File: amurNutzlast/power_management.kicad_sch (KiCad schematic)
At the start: 14 parts

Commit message: finisched design schematics + pdf
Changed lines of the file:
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@@
   (junction (at 157.48 96.52) (diameter 0) (color 0 0 0 0)
   )
+  (junction (at 177.8 63.5) (diameter 0) (color 0 0 0 0)
+  )
   (junction (at 147.32 96.52) (diameter 0) (color 0 0 0 0)
   )
@@
   (junction (at 45.72 73.66) (diameter 0) (color 0 0 0 0)
   )
+  (junction (at 177.8 96.52) (diameter 0) (color 0 0 0 0)
+  )
   (junction (at 132.08 78.74) (diameter 0) (color 0 0 0 0)
   )
@@
     (stroke (width 0) (type default))
   )
+  (wire (pts (xy 55.88 63.5) (xy 55.88 73.66))
+    (stroke (width 0) (type default))
+  )
   (wire (pts (xy 71.12 73.66) (xy 76.2 73.66))
     (stroke (width 0) (type default))
@@
     (stroke (width 0) (type default))
   )
+  (wire (pts (xy 177.8 96.52) (xy 187.96 96.52))
+    (stroke (width 0) (type default))
+  )
   (wire (pts (xy 71.12 81.28) (xy 71.12 78.74))
     (stroke (width 0) (type default))
@@
     (stroke (width 0) (type default))
   )
+  (wire (pts (xy 187.96 58.42) (xy 187.96 63.5))
+    (stroke (width 0) (type default))
+  )
   (wire (pts (xy 157.48 96.52) (xy 165.1 96.52))
     (stroke (width 0) (type default))
@@
     (stroke (width 0) (type default))
   )
+  (wire (pts (xy 177.8 63.5) (xy 187.96 63.5))
+    (stroke (width 0) (type default))
+  )
   (wire (pts (xy 63.5 73.66) (xy 63.5 86.36))
     (stroke (width 0) (type default))
@@
   )
   (wire (pts (xy 71.12 76.2) (xy 71.12 73.66))
+    (stroke (width 0) (type default))
+  )
+  (wire (pts (xy 187.96 91.44) (xy 187.96 96.52))
     (stroke (width 0) (type default))
   )
@@
     )
   )
+  (symbol (lib_id "power:PWR_FLAG") (at 187.96 91.44 0) (unit 1)
+    (in_bom yes) (on_board yes) (dnp no) (fields_autoplaced)
+    (property "Reference" "#FLG02" (at 187.96 89.535 0)
+      (effects (font (size 1.27 1.27)) hide)
+    )
+    (property "Value" "PWR_FLAG" (at 187.96 86.36 0)
+      (effects (font (size 1.27 1.27)))
+    )
+    (property "Footprint" "" (at 187.96 91.44 0)
+      (effects (font (size 1.27 1.27)) hide)
+    )
+    (property "Datasheet" "~" (at 187.96 91.44 0)
+      (effects (font (size 1.27 1.27)) hide)
+    )
+    (pin "1")
+    (instances
+      (project "amurNutzlast"
+        (path "/81bb76b1-eb1b-4eda-9d04-3f9c2ab6907c/c3ff46ef-9658-4832-9a1d-c566885b7e4f"
+          (reference "#FLG02") (unit 1)
+        )
+      )
+    )
+  )
+  (symbol (lib_id "power:PWR_FLAG") (at 187.96 58.42 0) (unit 1)
+    (in_bom yes) (on_board yes) (dnp no) (fields_autoplaced)
+    (property "Reference" "#FLG01" (at 187.96 56.515 0)
+      (effects (font (size 1.27 1.27)) hide)
+    )
+    (property "Value" "PWR_FLAG" (at 187.96 53.34 0)
+      (effects (font (size 1.27 1.27)))
+    )
+    (property "Footprint" "" (at 187.96 58.42 0)
+      (effects (font (size 1.27 1.27)) hide)
+    )
+    (property "Datasheet" "~" (at 187.96 58.42 0)
+      (effects (font (size 1.27 1.27)) hide)
+    )
+    (pin "1")
+    (instances
+      (project "amurNutzlast"
+        (path "/81bb76b1-eb1b-4eda-9d04-3f9c2ab6907c/c3ff46ef-9658-4832-9a1d-c566885b7e4f"
+          (reference "#FLG01") (unit 1)
+        )
+      )
+    )
+  )
   (symbol (lib_id "Device:R_Small") (at 132.08 68.58 0) (unit 1)
     (in_bom yes) (on_board yes) (dnp no) (fields_autoplaced)
@@
         )
       )
+    )
+  )
+  (symbol (lib_id "power:PWR_FLAG") (at 55.88 63.5 0) (unit 1)
+    (in_bom yes) (on_board yes) (dnp no) (fields_autoplaced)
+    (property "Reference" "#FLG010" (at 55.88 61.595 0)
+      (effects (font (size 1.27 1.27)) hide)
+    )
+    (property "Value" "PWR_FLAG" (at 55.88 58.42 0)
+      (effects (font (size 1.27 1.27)))
+    )
+    (property "Footprint" "" (at 55.88 63.5 0)
+      (effects (font (size 1.27 1.27)) hide)
+    )
+    (property "Datasheet" "~" (at 55.88 63.5 0)
+      (effects (font (size 1.27 1.27)) hide)
+    )
+    (pin "1")
+    (instances
+      (project "amurNutzlast"
+        (path "/81bb76b1-eb1b-4eda-9d04-3f9c2ab6907c/c3ff46ef-9658-4832-9a1d-c566885b7e4f"
+          (reference "#FLG010") (unit 1)
+        )
+      )

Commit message: layout start
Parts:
- C19, C20, C21, C22, C23: footprint (none) -> Capacitor_SMD:C_0603_1608Metric
- R10, R11, R12, R13, R14, R7, R8, R9: footprint (none) -> Resistor_SMD:R_0603_1608Metric
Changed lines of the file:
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@@
       (effects (font (size 1.27 1.27)) (justify left))
     )
-    (property "Footprint" "" (at 119.38 99.06 0)
+    (property "Footprint" "Capacitor_SMD:C_0603_1608Metric" (at 119.38 99.06 0)
       (effects (font (size 1.27 1.27)) hide)
     )
@@
       (effects (font (size 1.27 1.27)) (justify left))
     )
-    (property "Footprint" "" (at 63.5 88.9 0)
+    (property "Footprint" "Resistor_SMD:R_0603_1608Metric" (at 63.5 88.9 0)
       (effects (font (size 1.27 1.27)) hide)
     )
@@
       (effects (font (size 1.27 1.27)) (justify left))
     )
-    (property "Footprint" "" (at 45.72 81.28 0)
+    (property "Footprint" "Capacitor_SMD:C_0603_1608Metric" (at 45.72 81.28 0)
       (effects (font (size 1.27 1.27)) hide)
     )
@@
       (effects (font (size 1.27 1.27)))
     )
-    (property "Footprint" "" (at 167.64 96.52 0)
+    (property "Footprint" "Resistor_SMD:R_0603_1608Metric" (at 167.64 96.52 0)
       (effects (font (size 1.27 1.27)) hide)
     )
@@
       (effects (font (size 1.27 1.27)) (justify right))
     )
-    (property "Footprint" "" (at 160.02 71.12 0)
+    (property "Footprint" "Resistor_SMD:R_0603_1608Metric" (at 160.02 71.12 0)
       (effects (font (size 1.27 1.27)) hide)
     )
@@
       (effects (font (size 1.27 1.27)) (justify left))
     )
-    (property "Footprint" "" (at 55.88 88.9 0)
+    (property "Footprint" "Resistor_SMD:R_0603_1608Metric" (at 55.88 88.9 0)
       (effects (font (size 1.27 1.27)) hide)
     )
@@
       (effects (font (size 1.27 1.27)) (justify left))
     )
-    (property "Footprint" "" (at 119.38 66.04 0)
+    (property "Footprint" "Capacitor_SMD:C_0603_1608Metric" (at 119.38 66.04 0)
       (effects (font (size 1.27 1.27)) hide)
     )
@@
       (effects (font (size 1.27 1.27)) (justify left))
     )
-    (property "Footprint" "" (at 132.08 68.58 0)
+    (property "Footprint" "Resistor_SMD:R_0603_1608Metric" (at 132.08 68.58 0)
       (effects (font (size 1.27 1.27)) hide)
     )
@@
       (effects (font (size 1.27 1.27)))
     )
-    (property "Footprint" "" (at 170.18 63.5 0)
+    (property "Footprint" "Resistor_SMD:R_0603_1608Metric" (at 170.18 63.5 0)
       (effects (font (size 1.27 1.27)) hide)
     )
@@
       (effects (font (size 1.27 1.27)) (justify left))
     )
-    (property "Footprint" "" (at 157.48 104.14 0)
+    (property "Footprint" "Resistor_SMD:R_0603_1608Metric" (at 157.48 104.14 0)
       (effects (font (size 1.27 1.27)) hide)
     )
@@
       (effects (font (size 1.27 1.27)))
     )
-    (property "Footprint" "" (at 142.24 78.74 0)
+    (property "Footprint" "Resistor_SMD:R_0603_1608Metric" (at 142.24 78.74 0)
       (effects (font (size 1.27 1.27)) hide)
     )
@@
       (effects (font (size 1.27 1.27)) (justify left))
     )
-    (property "Footprint" "" (at 149.86 68.58 0)
+    (property "Footprint" "Capacitor_SMD:C_0603_1608Metric" (at 149.86 68.58 0)
       (effects (font (size 1.27 1.27)) hide)
     )
@@
       (effects (font (size 1.27 1.27)) (justify left))
     )
-    (property "Footprint" "" (at 147.32 104.14 0)
-      (effects (font (size 1.27 1.27)) hide)
-    )
+    (property "Footprint" "Capacitor_SMD:C_0603_1608Metric" (at 147.32 104.14 0)
+      (effects (font (size 1.27 1.27)) hide)
+    )

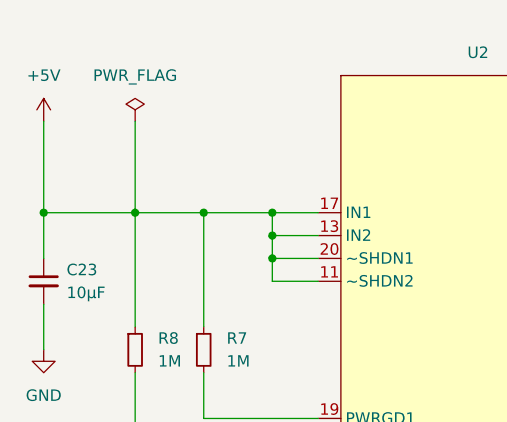
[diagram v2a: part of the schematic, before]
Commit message: deleted 3.3 converter for ftdi and moved USB to a hierarhical sheet
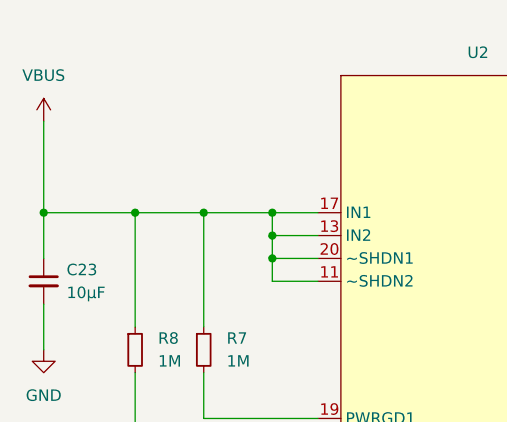
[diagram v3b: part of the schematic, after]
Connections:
- net +5V renamed VBUS
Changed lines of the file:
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@@
-    (stroke (width 0) (type default))
-  )
-  (wire (pts (xy 55.88 63.5) (xy 55.88 73.66))
     (stroke (width 0) (type default))
   )
@@
         (path "/81bb76b1-eb1b-4eda-9d04-3f9c2ab6907c/c3ff46ef-9658-4832-9a1d-c566885b7e4f"
           (reference "#PWR044") (unit 1)
-        )
-      )
-    )
-  )
-  (symbol (lib_id "power:+5V") (at 45.72 63.5 0) (unit 1)
-    (in_bom yes) (on_board yes) (dnp no) (fields_autoplaced)
-    (property "Reference" "#PWR043" (at 45.72 67.31 0)
-      (effects (font (size 1.27 1.27)) hide)
-    )
-    (property "Value" "+5V" (at 45.72 58.42 0)
-      (effects (font (size 1.27 1.27)))
-    )
-    (property "Footprint" "" (at 45.72 63.5 0)
-      (effects (font (size 1.27 1.27)) hide)
-    )
-    (property "Datasheet" "" (at 45.72 63.5 0)
-      (effects (font (size 1.27 1.27)) hide)
-    )
-    (pin "1")
-    (instances
-      (project "amurNutzlast"
-        (path "/81bb76b1-eb1b-4eda-9d04-3f9c2ab6907c/c3ff46ef-9658-4832-9a1d-c566885b7e4f"
-          (reference "#PWR043") (unit 1)
         )
       )
@@
     )
   )
-  (symbol (lib_id "power:PWR_FLAG") (at 55.88 63.5 0) (unit 1)
-    (in_bom yes) (on_board yes) (dnp no) (fields_autoplaced)
-    (property "Reference" "#FLG010" (at 55.88 61.595 0)
-      (effects (font (size 1.27 1.27)) hide)
-    )
-    (property "Value" "PWR_FLAG" (at 55.88 58.42 0)
-      (effects (font (size 1.27 1.27)))
-    )
-    (property "Footprint" "" (at 55.88 63.5 0)
-      (effects (font (size 1.27 1.27)) hide)
-    )
-    (property "Datasheet" "~" (at 55.88 63.5 0)
-      (effects (font (size 1.27 1.27)) hide)
-    )
-    (pin "1")
-    (instances
-      (project "amurNutzlast"
-        (path "/81bb76b1-eb1b-4eda-9d04-3f9c2ab6907c/c3ff46ef-9658-4832-9a1d-c566885b7e4f"
-          (reference "#FLG010") (unit 1)
-        )
-      )
+  (symbol (lib_id "power:VBUS") (at 45.72 63.5 0) (unit 1)
+    (in_bom yes) (on_board yes) (dnp no) (fields_autoplaced)
+    (property "Reference" "#PWR043" (at 45.72 67.31 0)
+      (effects (font (size 1.27 1.27)) hide)
+    )
+    (property "Value" "VBUS" (at 45.72 58.42 0)
+      (effects (font (size 1.27 1.27)))
+    )
+    (property "Footprint" "" (at 45.72 63.5 0)
+      (effects (font (size 1.27 1.27)) hide)
+    )
+    (property "Datasheet" "" (at 45.72 63.5 0)
+      (effects (font (size 1.27 1.27)) hide)
+    )
+    (pin "1")
+    (instances
+      (project "amurNutzlast"
+        (path "/81bb76b1-eb1b-4eda-9d04-3f9c2ab6907c/c3ff46ef-9658-4832-9a1d-c566885b7e4f"
+          (reference "#PWR043") (unit 1)
+        )
+      )

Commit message: layout ftdi placement
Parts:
- added C40: 0.1µF, Capacitor_SMD:C_0603_1608Metric, symbol Device:C_Small
- added C41: 10µF, Capacitor_SMD:C_0603_1608Metric, symbol Device:C_Small
- added U3: LD1117S33TR_SOT223, Package_TO_SOT_SMD:SOT-223-3_TabPin2, symbol Regulator_Linear:LD1117S33TR_SOT223
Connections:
- net VBUS: now also C40.1, U3.3 (VI); no longer C23.1, R7.1, R8.1, U2.11 (~SHDN2), U2.13 (IN2), U2.14 (IN2), U2.17 (IN1), U2.18 (IN1), U2.20 (~SHDN1)
- new net +3.3VP: C41.1, U3.2 (VO)
- new net +5V: C23.1, R7.1, R8.1, U2.11 (~SHDN2), U2.13 (IN2), U2.14 (IN2), U2.17 (IN1), U2.18 (IN1), U2.20 (~SHDN1)
- new net GND1: C40.2, C41.2, U3.1 (GND)

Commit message: placement finished
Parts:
- added J2: Conn_02x02_Counter_Clockwise, Connector_PinHeader_2.54mm:PinHeader_2x02_P2.54mm_Vertical, symbol Connector_Generic:Conn_02x02_Counter_Clockwise
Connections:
- net +5V: now also J2.2 (Pin_2)
- net GND: now also J2.4 (Pin_4)
- net GND1: now also J2.3 (Pin_3)
- net VBUS: now also J2.1 (Pin_1)
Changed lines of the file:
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@@
+    (stroke (width 0) (type default))
+  )
+  (wire (pts (xy 58.42 25.4) (xy 60.96 25.4))
     (stroke (width 0) (type default))
   )
@@
     (stroke (width 0) (type default))
   )
+  (wire (pts (xy 53.34 27.94) (xy 53.34 22.86))
+    (stroke (width 0) (type default))
+  )
   (wire (pts (xy 45.72 50.8) (xy 45.72 73.66))
     (stroke (width 0) (type default))
@@
     (stroke (width 0) (type default))
   )
+  (wire (pts (xy 81.28 30.48) (xy 81.28 25.4))
+    (stroke (width 0) (type default))
+  )
   (wire (pts (xy 73.66 157.48) (xy 81.28 157.48))
     (stroke (width 0) (type default))
@@
     (stroke (width 0) (type default))
   )
+  (wire (pts (xy 76.2 30.48) (xy 76.2 27.94))
+    (stroke (width 0) (type default))
+  )
   (wire (pts (xy 147.32 96.52) (xy 157.48 96.52))
     (stroke (width 0) (type default))
@@
     (stroke (width 0) (type default))
   )
+  (wire (pts (xy 76.2 27.94) (xy 73.66 27.94))
+    (stroke (width 0) (type default))
+  )
   (wire (pts (xy 73.66 165.1) (xy 73.66 167.64))
     (stroke (width 0) (type default))
@@
     (stroke (width 0) (type default))
   )
+  (wire (pts (xy 73.66 25.4) (xy 81.28 25.4))
+    (stroke (width 0) (type default))
+  )
   (wire (pts (xy 111.76 63.5) (xy 119.38 63.5))
     (stroke (width 0) (type default))
@@
     (stroke (width 0) (type default))
   )
+  (wire (pts (xy 53.34 27.94) (xy 60.96 27.94))
+    (stroke (width 0) (type default))
+  )
   (wire (pts (xy 129.54 96.52) (xy 147.32 96.52))
     (stroke (width 0) (type default))
   )
+  (wire (pts (xy 58.42 22.86) (xy 58.42 25.4))
+    (stroke (width 0) (type default))
+  )
   (wire (pts (xy 111.76 96.52) (xy 119.38 96.52))
     (stroke (width 0) (type default))
@@
         (path "/81bb76b1-eb1b-4eda-9d04-3f9c2ab6907c/c3ff46ef-9658-4832-9a1d-c566885b7e4f"
           (reference "C23") (unit 1)
+        )
+      )
+    )
+  )
+  (symbol (lib_id "power:VBUS") (at 58.42 22.86 0) (unit 1)
+    (in_bom yes) (on_board yes) (dnp no) (fields_autoplaced)
+    (property "Reference" "#PWR097" (at 58.42 26.67 0)
+      (effects (font (size 1.27 1.27)) hide)
+    )
+    (property "Value" "VBUS" (at 58.42 17.78 0)
+      (effects (font (size 1.27 1.27)))
+    )
+    (property "Footprint" "" (at 58.42 22.86 0)
+      (effects (font (size 1.27 1.27)) hide)
+    )
+    (property "Datasheet" "" (at 58.42 22.86 0)
+      (effects (font (size 1.27 1.27)) hide)
+    )
+    (pin "1")
+    (instances
+      (project "amurNutzlast"
+        (path "/81bb76b1-eb1b-4eda-9d04-3f9c2ab6907c/c3ff46ef-9658-4832-9a1d-c566885b7e4f"
+          (reference "#PWR097") (unit 1)
         )
       )
@@
     )
   )
+  (symbol (lib_id "Connector_Generic:Conn_02x02_Counter_Clockwise") (at 66.04 25.4 0) (unit 1)
+    (in_bom yes) (on_board yes) (dnp no)
+    (property "Reference" "J2" (at 67.31 19.05 0)
+      (effects (font (size 1.27 1.27)))
+    )
+    (property "Value" "Conn_02x02_Counter_Clockwise" (at 68.58 43.18 0)
+      (effects (font (size 1.27 1.27)))
+    )
+    (property "Footprint" "Connector_PinHeader_2.54mm:PinHeader_2x02_P2.54mm_Vertical" (at 66.04 25.4 0)
+      (effects (font (size 1.27 1.27)) hide)
+    )
+    (property "Datasheet" "~" (at 66.04 25.4 0)
+      (effects (font (size 1.27 1.27)) hide)
+    )
+    (pin "1")
+    (pin "2")
+    (pin "3")
+    (pin "4")
+    (instances
+      (project "amurNutzlast"
+        (path "/81bb76b1-eb1b-4eda-9d04-3f9c2ab6907c/c3ff46ef-9658-4832-9a1d-c566885b7e4f"
+          (reference "J2") (unit 1)
+        )
+      )
+    )
+  )
   (symbol (lib_id "power:GND") (at 157.48 114.3 0) (unit 1)
     (in_bom yes) (on_board yes) (dnp no) (fields_autoplaced)
@@
         (path "/81bb76b1-eb1b-4eda-9d04-3f9c2ab6907c/c3ff46ef-9658-4832-9a1d-c566885b7e4f"
           (reference "C39") (unit 1)
+        )
+      )
+    )
+  )
+  (symbol (lib_id "power:+5V") (at 53.34 22.86 0) (unit 1)
+    (in_bom yes) (on_board yes) (dnp no) (fields_autoplaced)
+    (property "Reference" "#PWR098" (at 53.34 26.67 0)
+      (effects (font (size 1.27 1.27)) hide)
+    )
+    (property "Value" "+5V" (at 53.34 17.78 0)
+      (effects (font (size 1.27 1.27)))
+    )
+    (property "Footprint" "" (at 53.34 22.86 0)
+      (effects (font (size 1.27 1.27)) hide)
+    )
+    (property "Datasheet" "" (at 53.34 22.86 0)
+      (effects (font (size 1.27 1.27)) hide)
+    )
+    (pin "1")
+    (instances
+      (project "amurNutzlast"
+        (path "/81bb76b1-eb1b-4eda-9d04-3f9c2ab6907c/c3ff46ef-9658-4832-9a1d-c566885b7e4f"
+          (reference "#PWR098") (unit 1)
         )
       )
@@
     )
   )
+  (symbol (lib_id "power:GND") (at 81.28 30.48 0) (unit 1)
+    (in_bom yes) (on_board yes) (dnp no) (fields_autoplaced)
+    (property "Reference" "#PWR099" (at 81.28 36.83 0)
+      (effects (font (size 1.27 1.27)) hide)
+    )
+    (property "Value" "GND" (at 81.28 35.56 0)
+      (effects (font (size 1.27 1.27)))
+    )
+    (property "Footprint" "" (at 81.28 30.48 0)
+      (effects (font (size 1.27 1.27)) hide)
+    )
+    (property "Datasheet" "" (at 81.28 30.48 0)
+      (effects (font (size 1.27 1.27)) hide)
+    )
+    (pin "1")
+    (instances
+      (project "amurNutzlast"
+        (path "/81bb76b1-eb1b-4eda-9d04-3f9c2ab6907c/c3ff46ef-9658-4832-9a1d-c566885b7e4f"
+          (reference "#PWR099") (unit 1)
+        )
+      )
+    )
+  )
   (symbol (lib_id "power:+5V") (at 45.72 50.8 0) (unit 1)
     (in_bom yes) (on_board yes) (dnp no) (fields_autoplaced)
@@
         )
       )
+    )
+  )
+  (symbol (lib_id "power:GND1") (at 76.2 30.48 0) (unit 1)
+    (in_bom yes) (on_board yes) (dnp no) (fields_autoplaced)
+    (property "Reference" "#PWR0100" (at 76.2 36.83 0)
+      (effects (font (size 1.27 1.27)) hide)
+    )
+    (property "Value" "GND1" (at 76.2 35.56 0)
+      (effects (font (size 1.27 1.27)))
+    )
+    (property "Footprint" "" (at 76.2 30.48 0)
+      (effects (font (size 1.27 1.27)) hide)
+    )
+    (property "Datasheet" "" (at 76.2 30.48 0)
+      (effects (font (size 1.27 1.27)) hide)
+    )
+    (pin "1")
+    (instances
+      (project "amurNutzlast"
+        (path "/81bb76b1-eb1b-4eda-9d04-3f9c2ab6907c/c3ff46ef-9658-4832-9a1d-c566885b7e4f"
+          (reference "#PWR0100") (unit 1)
+        )
+      )

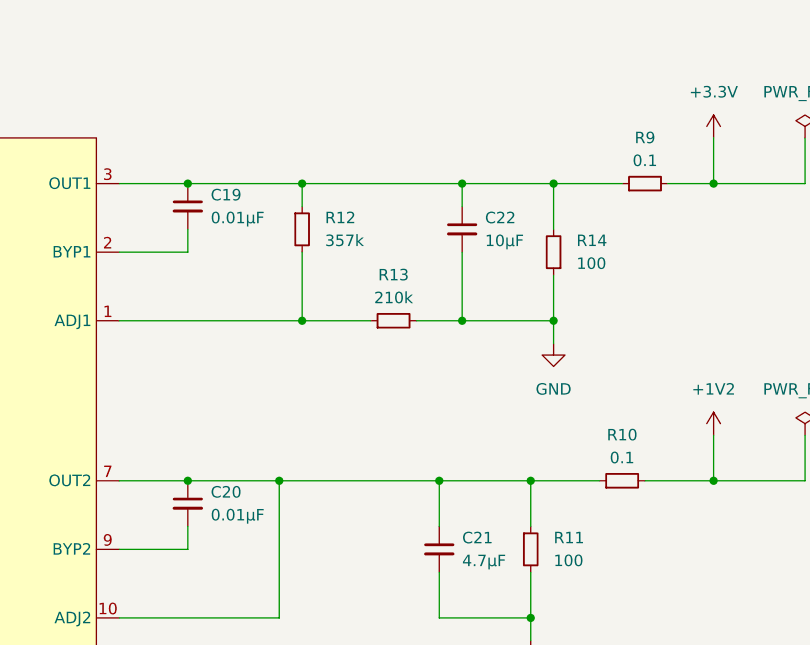
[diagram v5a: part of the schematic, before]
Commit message: gpio connected
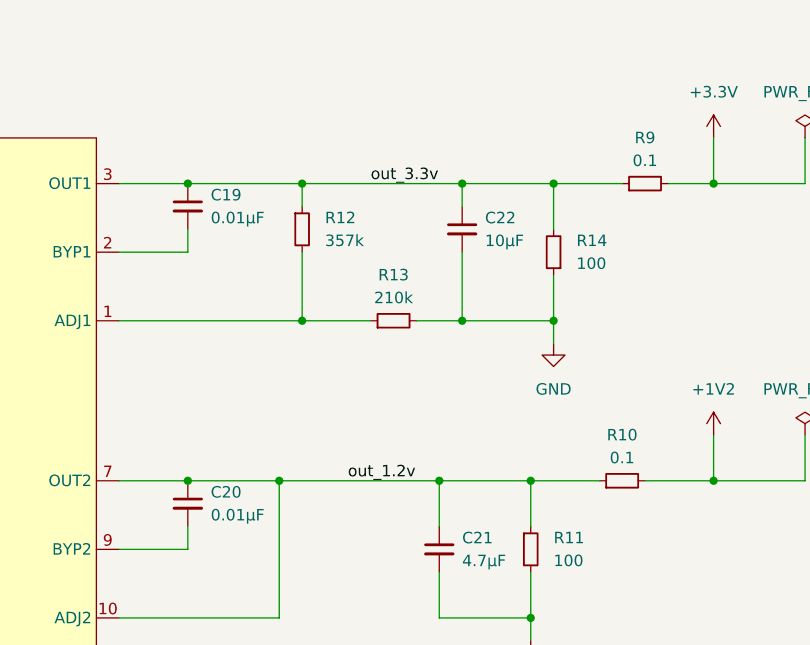
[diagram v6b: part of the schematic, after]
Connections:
- net out_1.2v: now reaches C20.1, C21.1, R10.1, R11.1, U2.10 (ADJ2), U2.7 (OUT2), U2.8 (OUT2)
- net out_3.3v: now reaches C19.1, C22.1, R12.1, R14.2, R9.1, U2.3 (OUT1), U2.4 (OUT1)
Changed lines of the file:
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@@
     (stroke (width 0) (type default))
+  )
+  (label "out_1.2v" (at 137.16 96.52 0) (fields_autoplaced)
+    (effects (font (size 1.27 1.27)) (justify left bottom))
+  )
+  (label "out_3.3v" (at 139.7 63.5 0) (fields_autoplaced)
+    (effects (font (size 1.27 1.27)) (justify left bottom))
   )
   (symbol (lib_id "Device:C_Small") (at 119.38 99.06 0) (unit 1)
